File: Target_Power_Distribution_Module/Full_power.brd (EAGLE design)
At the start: 64.4 x 39.4 mm, 28 parts, among them IC1 MCP1702, Q1 NFET, Q2 PFET, Q3 NFET, Q4 PFET

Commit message: Trace widths
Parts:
- moved SW1 2.54 mm to (16.5, 52.1)
- moved JP1 1.27 mm to (3.81, 54.6)
- moved SW2 1.27 mm to (24.1, 52.1)
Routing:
- net GND-ISO: track 176.9 -> 213.4 mm
- net 5V_RAW: track 11.9 -> 33.0 mm
- net N$6: track 103.7 -> 123.7 mm
- net SENSOR_POWER: track 31.3 -> 42.5 mm
- net 3.3V: track 77.4 -> 86.0 mm
- net N$2: track 27.0 -> 34.8 mm
- net 5V: track 130.7 -> 125.0 mm
- net N$4: track 58.8 -> 54.8 mm
- net 5V_SWITCH: track 18.7 -> 19.8 mm

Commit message: Some schematic updates
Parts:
- removed D2: TVS, SparkFun-DiscreteSemi:DIODE-ZENER
- added CNTRL_INPUTS: (no value), SparkFun-Connectors:1X02
- added D3: TVS, SparkFun-DiscreteSemi:DIODE-1N4001
- C3, C4: value 1 uF -> .1 uF
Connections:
- net 3.3V: now also STATE_CONTROLLER.1
- net 5V: now also D3.C; no longer D2.P$1, STATE_CONTROLLER.1
- net GND-ISO: now also D3.A; no longer D2.P$2
- net PI_PWR_CNTRL: now also CNTRL_INPUTS.2
- net SENSOR_PWR_CNTRL: now also CNTRL_INPUTS.1
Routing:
- net SENSOR_PWR_CNTRL: track 10.6 -> 45.3 mm
- net 3.3V: track 86.0 -> 113.6 mm
- net N$6: track 123.7 -> 100.1 mm
- net N$4: track 54.8 -> 75.3 mm
- net PI_PWR_CNTRL: track 9.33 -> 27.0 mm
- net 5V_RAW: track 33.0 -> 16.9 mm
- net GND-ISO: track 213.4 -> 200.7 mm
- net 5V: track 125.0 -> 114.5 mm
- net 5V_SWITCH: track 19.8 -> 26.8 mm

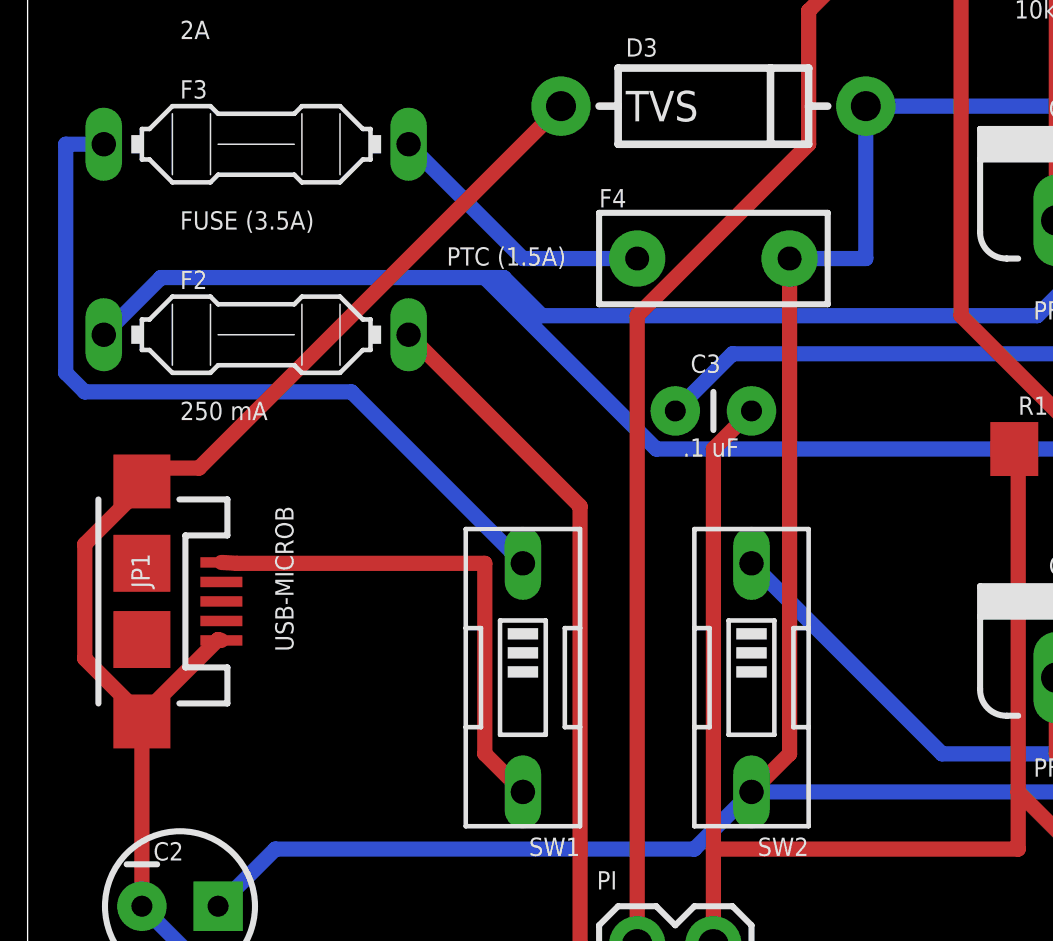
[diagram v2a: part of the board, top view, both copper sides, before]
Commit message: Some schematic updates, spi test is working
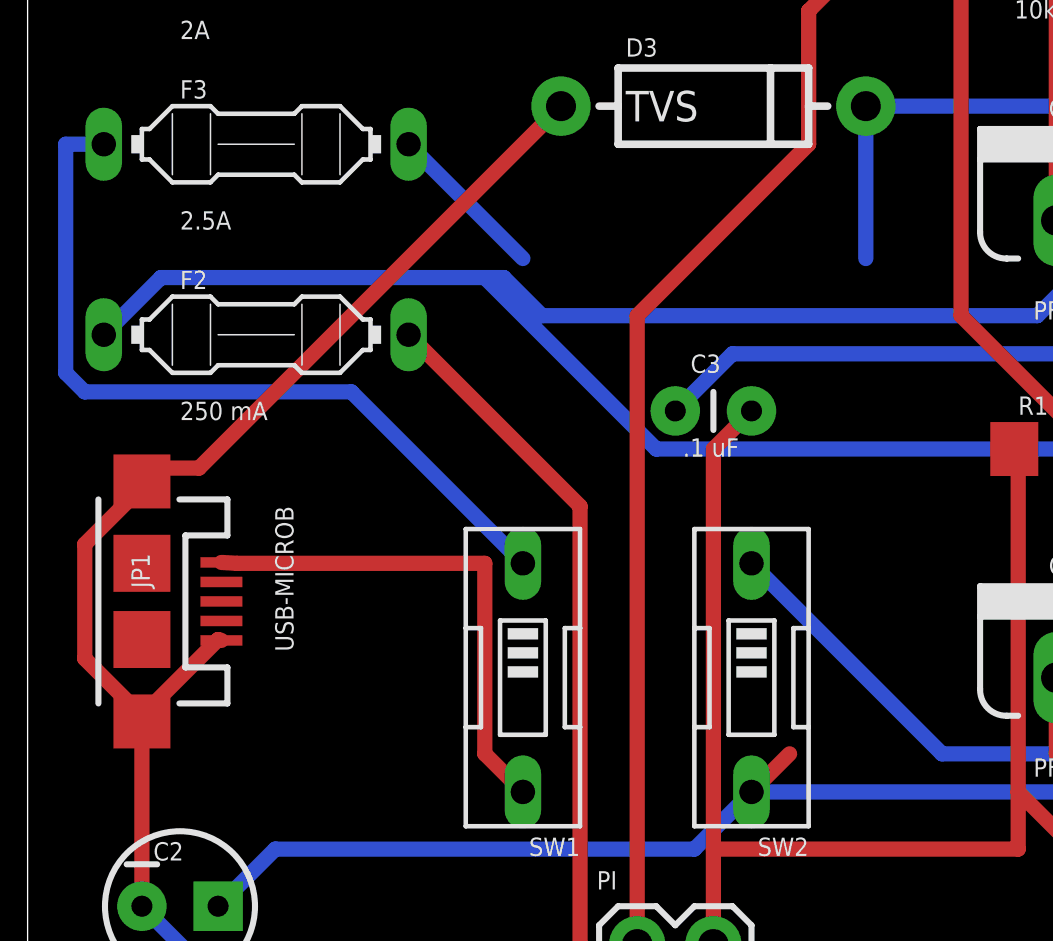
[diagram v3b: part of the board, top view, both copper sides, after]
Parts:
- removed F4: PTC (1.5A), SparkFun-PowerIC:PTC
- F3: value FUSE (3.5A) -> 2.5A
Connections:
- removed net N$7: F3.2, F4.P$1
- net 5V: now also F3.2; no longer F4.P$2
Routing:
- net 5V: track 114.5 -> 100.8 mm
- net N$7: track 9.20 -> 0.00 mm
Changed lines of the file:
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@@
 <attribute name="VALUE" x="5.08" y="60.6552" size="0.6096" layer="25" ratio="10"/>
 </element>
-<element name="F3" library="fuse" package="PICOFUSE" value="FUSE (3.5A)" x="7.62" y="69.85" smashed="yes">
+<element name="F3" library="fuse" package="PICOFUSE" value="2.5A" x="7.62" y="69.85" smashed="yes">
 <attribute name="OC_NEWARK" value="unknown" x="7.62" y="69.85" size="1.778" layer="27" display="off"/>
 <attribute name="MPN" value="" x="7.62" y="69.85" size="1.778" layer="27" display="off"/>
@@
 <attribute name="NAME" x="5.08" y="71.374" size="0.6096" layer="25" ratio="10"/>
 <attribute name="VALUE" x="5.08" y="67.0052" size="0.6096" layer="25" ratio="10"/>
-</element>
-<element name="F4" library="SparkFun-PowerIC" package="PTC" value="PTC (1.5A)" x="22.86" y="66.04" smashed="yes">
-<attribute name="NAME" x="19.05" y="67.745" size="0.6096" layer="25"/>
-<attribute name="VALUE" x="13.97" y="65.805" size="0.6096" layer="25"/>
 </element>
 <element name="IC1" library="adafruit" package="TO92" value="MCP1702" x="59.69" y="76.2" smashed="yes">
@@
 <contactref element="IC1" pad="2"/>
 <contactref element="C4" pad="1"/>
-<contactref element="F4" pad="P$2"/>
 <contactref element="C2" pad="1"/>
 <contactref element="C1" pad="1"/>
@@
 <wire x1="43.18" y1="59.69" x2="43.31" y2="59.69" width="0.508" layer="1"/>
 <wire x1="25.4" y1="49.53" x2="24.13" y2="48.26" width="0.508" layer="1"/>
-<wire x1="25.4" y1="66.04" x2="25.4" y2="49.53" width="0.508" layer="1"/>
 <wire x1="8.255" y1="46.355" x2="6.35" y2="44.45" width="0.508" layer="16"/>
 <wire x1="22.225" y1="46.355" x2="8.255" y2="46.355" width="0.508" layer="16"/>
 <wire x1="24.13" y1="48.26" x2="22.225" y2="46.355" width="0.508" layer="16"/>
 <wire x1="27.94" y1="66.04" x2="27.94" y2="71.12" width="0.508" layer="16"/>
-<wire x1="25.4" y1="66.04" x2="27.94" y2="66.04" width="0.508" layer="16"/>
 <wire x1="35.56" y1="48.26" x2="39.37" y2="52.07" width="0.508" layer="16"/>
 <wire x1="24.13" y1="48.26" x2="35.56" y2="48.26" width="0.508" layer="16"/>
 <wire x1="27.94" y1="71.12" x2="58.42" y2="71.12" width="0.508" layer="16"/>
+<contactref element="F3" pad="2"/>
+<wire x1="16.51" y1="66.04" x2="12.7" y2="69.85" width="0.508" layer="16"/>
+<wire x1="16.51" y1="66.04" x2="27.94" y2="66.04" width="0" layer="19" extent="16-16"/>
+<wire x1="39.37" y1="55.88" x2="27.94" y2="66.04" width="0" layer="19" extent="1-16"/>
 </signal>
 <signal name="SENSOR_PWR_CNTRL">
@@
 <wire x1="35.56" y1="43.18" x2="35.56" y2="41.275" width="0.508" layer="1"/>
 </signal>
-<signal name="N$7">
-<contactref element="F3" pad="2"/>
-<contactref element="F4" pad="P$1"/>
-<wire x1="16.51" y1="66.04" x2="12.7" y2="69.85" width="0.508" layer="16"/>
-<wire x1="20.32" y1="66.04" x2="16.51" y2="66.04" width="0.508" layer="16"/>
-</signal>
 <signal name="5V_RAW">

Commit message: Cleaned sensor on full schem
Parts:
- R1, R2, R3, R4, R5, R6: device SparkFun-Resistors:1206 -> adafruit:R1206
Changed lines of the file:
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@@
 <attribute name="VALUE" x="33.528" y="64.008" size="0.6096" layer="25" ratio="10"/>
 </element>
-<element name="R1" library="SparkFun-Resistors" package="1206" value="10k" x="34.29" y="59.69" smashed="yes">
+<element name="R1" library="adafruit" package="R1206" value="10k" x="34.29" y="59.69" smashed="yes">
 <attribute name="NAME" x="33.02" y="60.833" size="0.6096" layer="25"/>
 <attribute name="VALUE" x="34.163" y="57.531" size="0.6096" layer="25"/>
 </element>
-<element name="R2" library="SparkFun-Resistors" package="1206" value="10k" x="41.91" y="59.69" smashed="yes">
+<element name="R2" library="adafruit" package="R1206" value="10k" x="41.91" y="59.69" smashed="yes">
 <attribute name="NAME" x="40.64" y="60.833" size="0.6096" layer="25"/>
 <attribute name="VALUE" x="40.513" y="57.531" size="0.6096" layer="25"/>
 </element>
-<element name="R3" library="SparkFun-Resistors" package="1206" value="10k" x="49.53" y="59.69" smashed="yes">
+<element name="R3" library="adafruit" package="R1206" value="10k" x="49.53" y="59.69" smashed="yes">
 <attribute name="NAME" x="48.26" y="60.833" size="0.6096" layer="25"/>
 <attribute name="VALUE" x="48.133" y="57.531" size="0.6096" layer="25"/>
 </element>
-<element name="R4" library="SparkFun-Resistors" package="1206" value="10k" x="49.53" y="76.2" smashed="yes">
+<element name="R4" library="adafruit" package="R1206" value="10k" x="49.53" y="76.2" smashed="yes">
 <attribute name="NAME" x="48.26" y="77.343" size="0.6096" layer="25"/>
 <attribute name="VALUE" x="48.133" y="74.041" size="0.6096" layer="25"/>
 </element>
-<element name="R5" library="SparkFun-Resistors" package="1206" value="10k" x="41.91" y="76.2" smashed="yes">
+<element name="R5" library="adafruit" package="R1206" value="10k" x="41.91" y="76.2" smashed="yes">
 <attribute name="NAME" x="40.64" y="77.343" size="0.6096" layer="25"/>
 <attribute name="VALUE" x="40.513" y="74.041" size="0.6096" layer="25"/>
 </element>
-<element name="R6" library="SparkFun-Resistors" package="1206" value="10k" x="34.29" y="76.2" smashed="yes">
+<element name="R6" library="adafruit" package="R1206" value="10k" x="34.29" y="76.2" smashed="yes">
 <attribute name="NAME" x="33.02" y="77.343" size="0.6096" layer="25"/>
 <attribute name="VALUE" x="32.893" y="74.041" size="0.6096" layer="25"/>
@@
 <wire x1="33.02" y1="48.26" x2="33.02" y2="59.69" width="0.508" layer="1"/>
 <wire x1="38.1" y1="43.18" x2="33.02" y2="48.26" width="0.508" layer="1"/>
-<wire x1="33.02" y1="59.69" x2="32.89" y2="59.69" width="0.508" layer="1"/>
+<wire x1="33.02" y1="59.69" x2="32.868" y2="59.69" width="0.508" layer="1"/>
 <wire x1="33.02" y1="46.355" x2="22.86" y2="46.355" width="0.508" layer="1"/>
 <wire x1="33.02" y1="48.26" x2="33.02" y2="46.355" width="0.508" layer="1"/>
@@
 <wire x1="50.8" y1="62.23" x2="48.26" y2="59.69" width="0.508" layer="1"/>
 <wire x1="52.07" y1="67.31" x2="52.07" y2="63.5" width="0.508" layer="1"/>
-<wire x1="48.26" y1="59.69" x2="48.13" y2="59.69" width="0.508" layer="1"/>
+<wire x1="48.26" y1="59.69" x2="48.108" y2="59.69" width="0.508" layer="1"/>
 <wire x1="52.705" y1="43.815" x2="52.705" y2="51.435" width="0.508" layer="1"/>
 <wire x1="53.34" y1="43.18" x2="52.705" y2="43.815" width="0.508" layer="1"/>
@@
 <wire x1="47.625" y1="78.105" x2="42.545" y2="78.105" width="0.508" layer="1"/>
 <wire x1="47.625" y1="76.2" x2="47.625" y2="78.105" width="0.508" layer="1"/>
-<wire x1="40.64" y1="76.2" x2="40.51" y2="76.2" width="0.508" layer="1"/>
-<wire x1="47.625" y1="76.2" x2="48.13" y2="76.2" width="0.508" layer="1"/>
+<wire x1="40.64" y1="76.2" x2="40.488" y2="76.2" width="0.508" layer="1"/>
+<wire x1="47.625" y1="76.2" x2="48.108" y2="76.2" width="0.508" layer="1"/>
 <wire x1="60.96" y1="71.12" x2="60.96" y2="66.04" width="0.508" layer="1"/>
 <wire x1="58.42" y1="72.39" x2="58.42" y2="76.2" width="0.508" layer="16"/>
@@
 <wire x1="34.29" y1="49.53" x2="36.83" y2="49.53" width="0.508" layer="1"/>
 <wire x1="34.29" y1="52.07" x2="34.29" y2="49.53" width="0.508" layer="1"/>
-<wire x1="40.005" y1="59.69" x2="40.51" y2="59.69" width="0.508" layer="1"/>
+<wire x1="40.005" y1="59.69" x2="40.488" y2="59.69" width="0.508" layer="1"/>
 <wire x1="46.99" y1="54.61" x2="49.53" y2="52.07" width="0.508" layer="16"/>
 <wire x1="36.83" y1="54.61" x2="46.99" y2="54.61" width="0.508" layer="16"/>
@@
 <wire x1="46.99" y1="55.88" x2="50.8" y2="59.69" width="0.508" layer="1"/>
 <wire x1="46.99" y1="52.07" x2="46.99" y2="55.88" width="0.508" layer="1"/>
-<wire x1="50.8" y1="59.69" x2="50.93" y2="59.69" width="0.508" layer="1"/>
+<wire x1="50.8" y1="59.69" x2="50.952" y2="59.69" width="0.508" layer="1"/>
 <wire x1="54.61" y1="49.53" x2="60.96" y2="43.18" width="0.508" layer="16"/>
 <wire x1="49.53" y1="49.53" x2="54.61" y2="49.53" width="0.508" layer="16"/>
@@
 <wire x1="36.83" y1="59.055" x2="36.195" y2="59.69" width="0.508" layer="1"/>
 <wire x1="36.83" y1="52.07" x2="36.83" y2="59.055" width="0.508" layer="1"/>
-<wire x1="36.195" y1="59.69" x2="35.69" y2="59.69" width="0.508" layer="1"/>
+<wire x1="36.195" y1="59.69" x2="35.712" y2="59.69" width="0.508" layer="1"/>
 <wire x1="30.48" y1="49.53" x2="24.13" y2="55.88" width="0.508" layer="16"/>
 <wire x1="34.29" y1="49.53" x2="30.48" y2="49.53" width="0.508" layer="16"/>
@@
 <wire x1="31.115" y1="64.135" x2="31.115" y2="78.105" width="0.508" layer="1"/>
 <wire x1="35.56" y1="59.69" x2="31.115" y2="64.135" width="0.508" layer="1"/>
-<wire x1="35.56" y1="59.69" x2="35.69" y2="59.69" width="0.508" layer="1"/>
+<wire x1="35.56" y1="59.69" x2="35.712" y2="59.69" width="0.508" layer="1"/>
 </signal>
 <signal name="N$5">
@@
 <wire x1="34.29" y1="74.93" x2="33.02" y2="76.2" width="0.508" layer="1"/>
 <wire x1="34.29" y1="67.31" x2="34.29" y2="74.93" width="0.508" layer="1"/>
-<wire x1="33.02" y1="76.2" x2="32.89" y2="76.2" width="0.508" layer="1"/>
+<wire x1="33.02" y1="76.2" x2="32.868" y2="76.2" width="0.508" layer="1"/>
 <wire x1="46.99" y1="69.85" x2="49.53" y2="67.31" width="0.508" layer="16"/>
 <wire x1="36.83" y1="69.85" x2="46.99" y2="69.85" width="0.508" layer="16"/>
@@
 <wire x1="39.37" y1="64.77" x2="36.83" y2="64.77" width="0.508" layer="1"/>
 <wire x1="39.37" y1="66.04" x2="39.37" y2="64.77" width="0.508" layer="1"/>
-<wire x1="35.56" y1="76.2" x2="35.69" y2="76.2" width="0.508" layer="1"/>
+<wire x1="35.56" y1="76.2" x2="35.712" y2="76.2" width="0.508" layer="1"/>
 <wire x1="23.495" y1="62.865" x2="21.59" y2="60.96" width="0.508" layer="16"/>
 <wire x1="34.925" y1="62.865" x2="23.495" y2="62.865" width="0.508" layer="16"/>
@@
 <wire x1="39.37" y1="55.88" x2="43.18" y2="59.69" width="0.508" layer="1"/>
 <wire x1="39.37" y1="52.07" x2="39.37" y2="55.88" width="0.508" layer="1"/>
-<wire x1="43.18" y1="59.69" x2="43.31" y2="59.69" width="0.508" layer="1"/>
+<wire x1="43.18" y1="59.69" x2="43.332" y2="59.69" width="0.508" layer="1"/>
 <wire x1="25.4" y1="49.53" x2="24.13" y2="48.26" width="0.508" layer="1"/>
 <wire x1="8.255" y1="46.355" x2="6.35" y2="44.45" width="0.508" layer="16"/>
@@
 <wire x1="48.26" y1="73.66" x2="50.8" y2="76.2" width="0.508" layer="1"/>
 <wire x1="46.99" y1="67.31" x2="46.99" y2="72.39" width="0.508" layer="1"/>
-<wire x1="50.8" y1="76.2" x2="50.93" y2="76.2" width="0.508" layer="1"/>
+<wire x1="50.8" y1="76.2" x2="50.952" y2="76.2" width="0.508" layer="1"/>
 <wire x1="53.975" y1="47.625" x2="58.42" y2="43.18" width="0.508" layer="1"/>
 <wire x1="53.975" y1="67.945" x2="53.975" y2="47.625" width="0.508" layer="1"/>
@@
 <wire x1="36.83" y1="69.85" x2="43.18" y2="76.2" width="0.508" layer="1"/>
 <wire x1="36.83" y1="67.31" x2="36.83" y2="69.85" width="0.508" layer="1"/>
-<wire x1="43.18" y1="76.2" x2="43.31" y2="76.2" width="0.508" layer="1"/>
+<wire x1="43.18" y1="76.2" x2="43.332" y2="76.2" width="0.508" layer="1"/>
 <wire x1="4.445" y1="65.405" x2="2.54" y2="63.5" width="0.508" layer="16"/>
 <wire x1="15.875" y1="65.405" x2="15.24" y2="65.405" width="0.508" layer="16"/>
